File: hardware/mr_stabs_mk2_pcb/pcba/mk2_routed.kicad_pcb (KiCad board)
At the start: 4 copper layers, 93.2 x 35 mm, 73 parts, among them U1 INA228, U2 TPS54202DDC, U3 AP2112K-3.3, U4 BNO055, U5 USBLC6-2SC6, Y1 32.768kHz

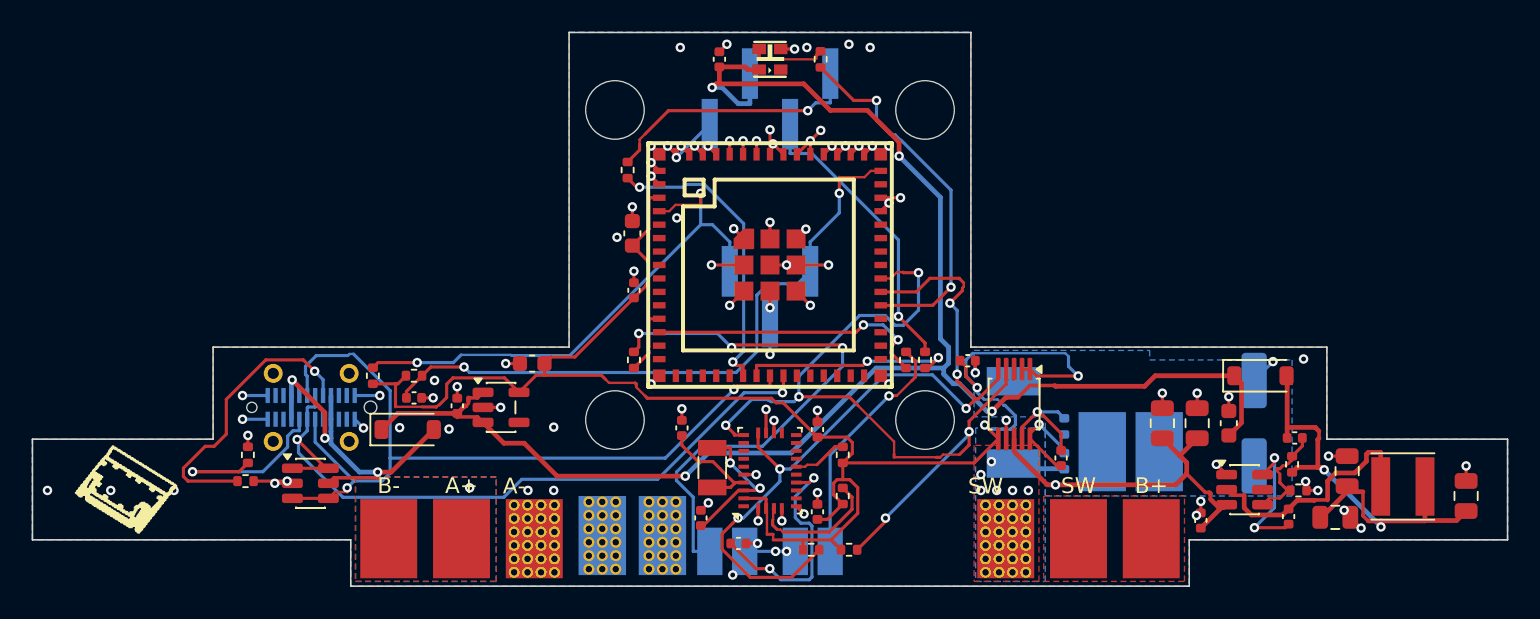
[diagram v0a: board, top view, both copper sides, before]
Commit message: Stand the Nano RX on a right-angle header and align the STEP models
- H2 is now an HX PZ2.54-1x4P WT right-angle SMD header (C46061677) at the stem's rear, pins
  pointing forward; the RX slides on and stands 18 mm toward the wedge. A vertical header would
  have laid it flat. Rotated 180 deg because KiCad mirrors bottom-side footprints and
  legalize.py does not; at 0 deg its pins pointed out past the rear edge.
- EasyEDA's footprints now use their STEP models, offset to match the VRML the renders use
  (align_models.py): the USB-C's STEP sat 2.55 mm low and the headers' 2.5 to 3.8 mm along the
  row, so the exported STEP disagreed with the render.
- New build123d model of the right-angle header; datasheet review for H2.
- Re-routed: 0 errors, 0 unconnected. Order files, STEP and simulations regenerated.

Co-Authored-By: Claude Opus 5.5 <noreply@anthropic.com>
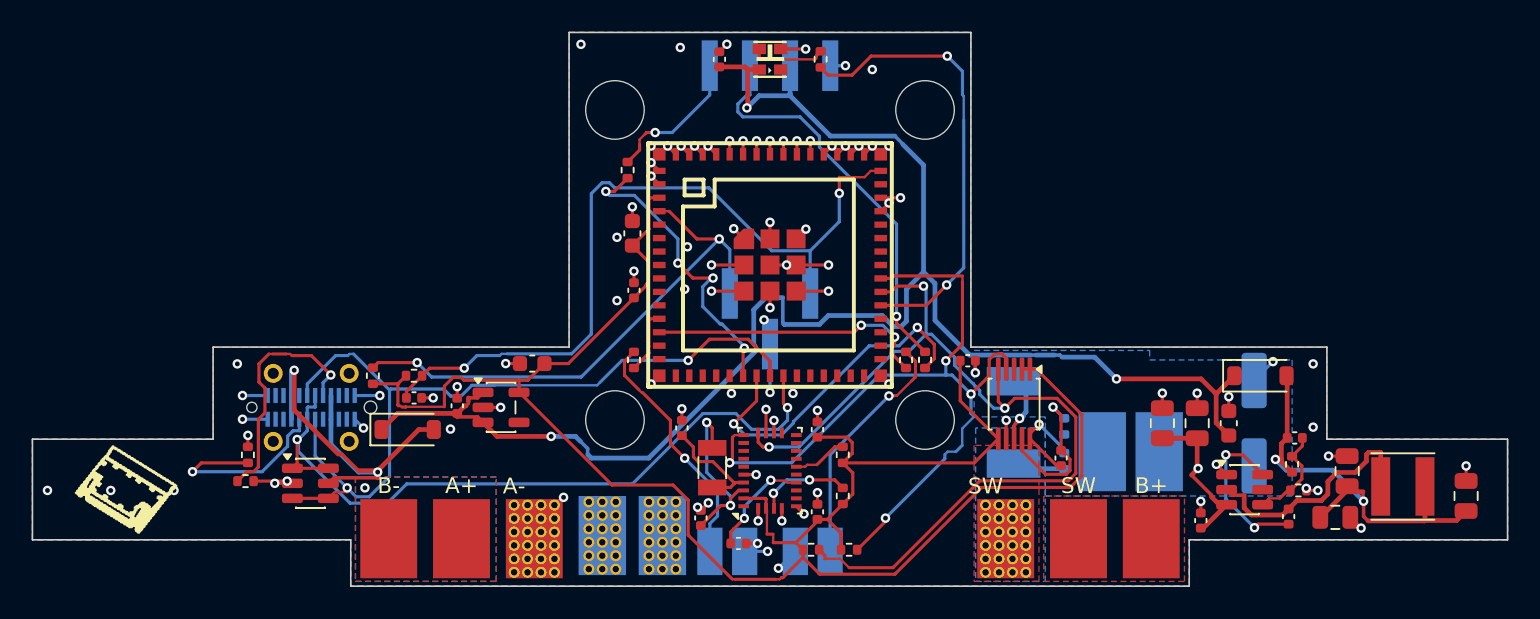
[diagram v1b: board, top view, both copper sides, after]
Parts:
- H2: footprint mk2:CONN-SMD_HX-PZ2.54-1X4P-TP-YQ -> mk2:CONN-SMD_HX-PZ2.54-1X4P-WT
- moved H2 2.10 mm to (100.0, 87.4), turned to 180 degrees
- moved H1 1.40 mm to (100.0, 103.4)
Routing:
- net DSHOT_L: track 35.6 -> 15.5 mm, vias 3 -> 1
- net +3V3: track 108.4 -> 122.4 mm, vias 3 -> 0
- net VBATT: track 22.8 -> 13.3 mm, vias 1 -> 2
- net SCL1: track 49.9 -> 58.3 mm, vias 5 -> 3
- net EN: track 41.0 -> 49.3 mm
- net IO18: track 13.5 -> 21.7 mm
- net IMU_CAP: track 14.9 -> 6.73 mm
- net CRSF_RX_RX: track 16.6 -> 9.19 mm
- net CRSF_RX_TX: track 18.7 -> 25.5 mm
- net IO39: track 23.2 -> 28.8 mm
- net VBUS_USB: track 22.5 -> 27.7 mm, vias 3 -> 2
- net USB_CC2: track 18.5 -> 15.4 mm
- net SENSE_N: track 7.16 -> 9.96 mm
- net IMU_BOOTLOAD: track 8.50 -> 5.92 mm, vias 0 -> 2
- net V5_BUCK: track 30.4 -> 28.0 mm
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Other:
- board text added: "C1"
- board text added: "C2"
- board text added: "NANO RX"
- board text removed: "1"
- board text removed: "2"
- board text removed: "NANO RX: 1=RX TX, 2=RX RX"

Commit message: Move the Mk2 USB-C and bulk cap into the stem; swap to INA238 and TYPE-C-31-D-06
- USB-C and the 100 uF bulk cap sit in the stem between the bosses, away from the motors under
  the ears. BOOT/RST moved to the left ear, the BNO055 block front-right of the USB-C's shell
  legs; two caps went to the wedge face under the parts they serve (no GND via room on top);
  two fixed GND stitching vias keep the stem's bottom pour joined.
- JLCPCB assembly had no INA228 and flagged the 24-pin USB-C as hard to source: INA238
  (C2868250, same pinout, 16-bit) and HRO TYPE-C-31-D-06 (C2689964, 16-pin USB 2.0), both
  reviewed against their datasheets. Paste in the USB-C's shell slots so reflow solders them.
- Re-routed: 0 errors, 0 unconnected. Order files (ORDER.md: PCBA Qty 2), STEP, schematic and
  simulations regenerated.

Firmware: the INA238 needs device ID 0x238, 16-bit reads, ADCRANGE 1 and SHUNT_OHMS 0.0005.

Co-Authored-By: Claude Opus 5.5 <noreply@anthropic.com>
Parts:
- added TP15: GND_STITCH, mk2:StitchVia_0.6mm, F.Cu at (111.6, 102.6)
- added TP16: GND_STITCH, mk2:StitchVia_0.6mm, F.Cu at (88.4, 102.6)
- C19, C22: moved to B.Cu
- U1: value INA228 -> INA238
- USB1: value TYPE-C-31-M-06 -> TYPE-C-31-D-06; footprint mk2:TYPE-C-USB-SMD_TYPE-C-31-M-06 -> mk2:USB-C-SMD_TYPE-C-31-D-06
- moved R16 33.2 mm to (100.0, 112.0)
- moved R15 33.0 mm to (100.0, 110.6), turned to 0 degrees
- moved C3 31.2 mm to (100.0, 104.0), turned to 180 degrees
- moved USB1 29.1 mm to (100.0, 111.1)
- moved U5 26.4 mm to (97.2, 116.1), turned to 180 degrees
- moved H1 21.7 mm to (79.0, 109.0)
- moved C23 11.7 mm to (105.5, 114.0), turned to 0 degrees
- moved C20 10.2 mm to (111.7, 115.9), turned to 180 degrees
- moved C19 9.61 mm to (107.6, 117.2)
- moved U4 8.77 mm to (107.5, 117.6), turned to 180 degrees
- moved Y1 7.62 mm to (103.1, 116.3)
- moved R12 7.60 mm to (111.4, 118.0)
- moved C22 7.51 mm to (103.1, 115.2), turned to 0 degrees
- moved D2 7.11 mm to (84.0, 112.2)
- moved R8 6.22 mm to (98.8, 118.5), turned to 180 degrees
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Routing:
- net USB_DM: track 52.9 -> 16.9 mm
- net SDA1: track 50.4 -> 73.5 mm
- net VBATT: track 13.3 -> 34.5 mm, vias 2 -> 4
- net SCL1: track 58.3 -> 39.0 mm, vias 3 -> 2
- net DSHOT_L: track 15.5 -> 34.1 mm
- net USB_DP: track 46.7 -> 29.3 mm
- net XOUT32: track 7.06 -> 20.4 mm, vias 0 -> 2
- net +3V3: track 122.4 -> 109.5 mm, vias 0 -> 8
- net IO18: track 21.7 -> 13.3 mm
- net +5V: track 103.9 -> 111.8 mm, vias 3 -> 4
- net XIN32: track 11.5 -> 19.2 mm
- net USB_CC2: track 15.4 -> 7.99 mm, vias 1 -> 3
- net GND: track 75.9 -> 69.3 mm, vias 94 -> 99
- net EN: track 49.3 -> 43.1 mm, vias 2 -> 6
- net IMU_BOOTLOAD: track 5.92 -> 1.60 mm, vias 2 -> 0
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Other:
- board text removed: "USB"

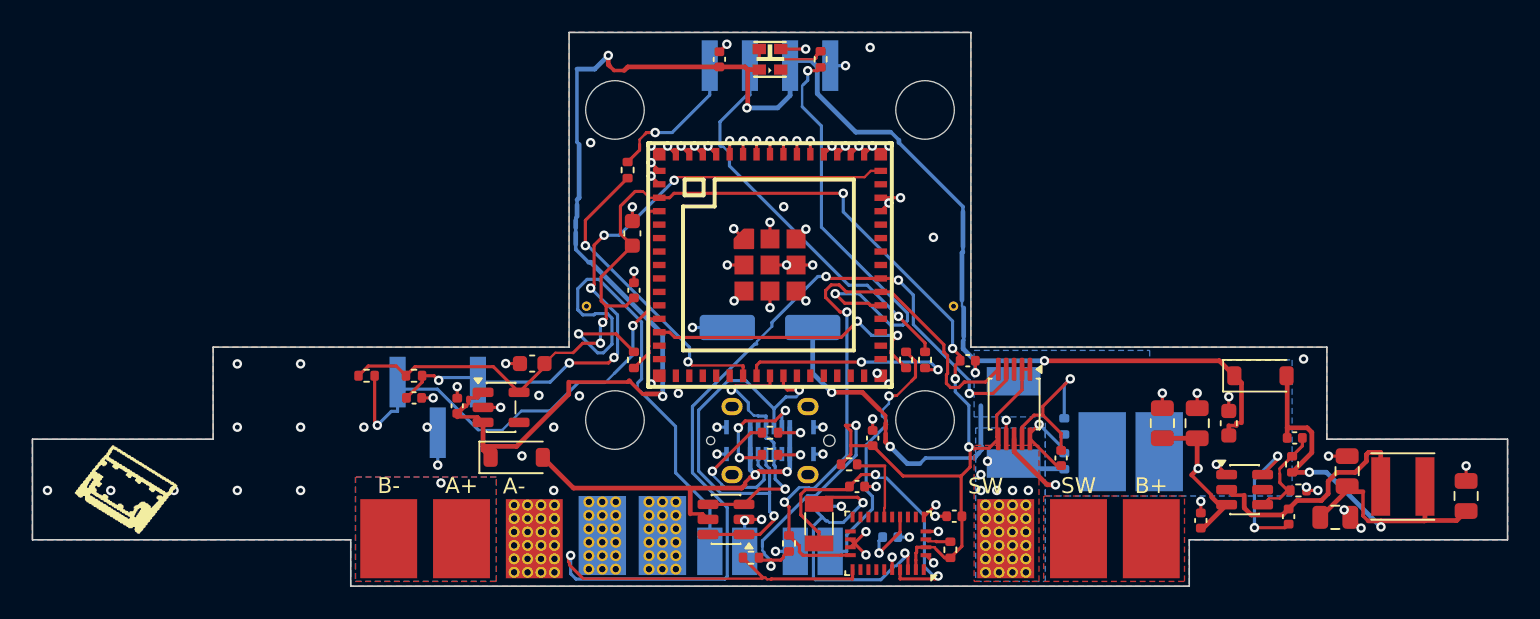
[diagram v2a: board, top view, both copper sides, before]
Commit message: Mk2 board v1.0: inner planes in the gerbers, signature, rounded corners, wired schematic
- gerbers.zip now has In1 and In2. fab.sh exported only F.Cu and B.Cu, so every earlier zip
  for this 4-layer board was missing both GND planes. ORDER.md says to check for 4 copper
  files.
- Silkscreen: "MR STABS MK2" and "v1.0 BEN W 2026" replace the XT60 pad legend on the bottom
  left ear (the roof-face pads keep their own labels), with the BWBots logo above them.
  VERSION in silk.py sets the revision.
- Convex outline corners filleted to 1 mm (corner_radius in gen_placement.py). Placement and
  routing unchanged; zones refilled. DRC 0 errors, 0 unconnected.
- Schematic redrawn as three hierarchical sheets (power, MCU and USB, IMU and radio) with
  nets as wires; connectivity matches mk2.net on all 37 nets.
- STEP, BOM, CPL and renders regenerated from the same board.

Co-Authored-By: Claude Opus 5.5 <noreply@anthropic.com>
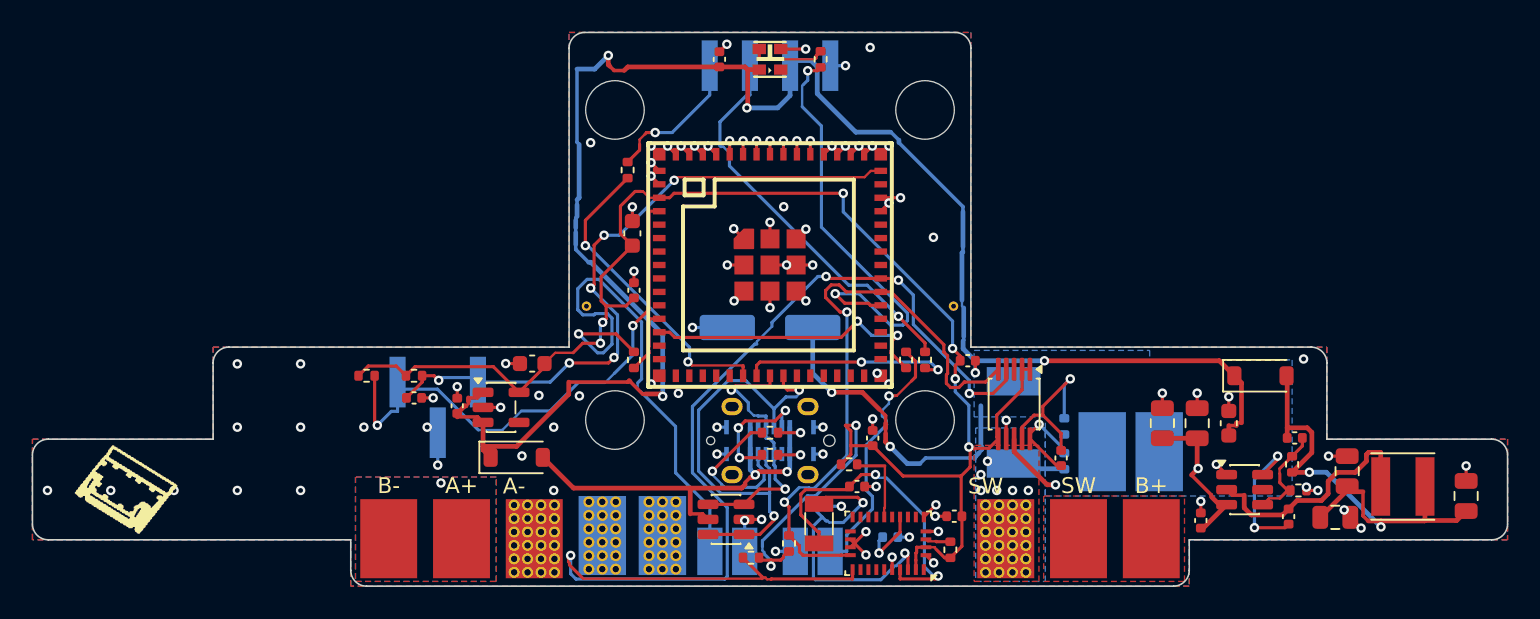
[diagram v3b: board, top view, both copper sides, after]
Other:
- outline, holes or cut-outs redrawn
- board text added: "v1.0 BEN W 2026"
- board text removed: "A-/A+ PACK A"
- board text removed: "B-/B+ PACK B"
- board text removed: "SW/SW SWITCH"
- board text removed: "XT60 PADS, TOP:"

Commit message: Re-route the Mk2 board at JLCPCB's 2 oz rules and fit the CPL rotations
The board orders with 2 oz outer copper, but it was routed at 0.15 mm clearance, a 1 oz
number. Against JLCPCB's 2 oz minimums (0.16 mm track, 0.20 mm space) it had 292 violations
behind a clean DRC. Re-routed at 0.20 mm: 0 errors, 0 unconnected, with mk2_routed.kicad_dru
holding the 2 oz rules so the KiCad GUI checks the same thing.

Getting the stem to route at 0.20 mm took these changes:
- Signal vias 0.5 / 0.25 mm; GND, battery and 5 V vias stay 0.6 / 0.3. Min hole 0.25 mm.
- C3 (100 uF bulk) back on the right ear beside the shunt. Its feed across the stem never
  routed at 2 oz spacing, and a prewired track there walled off the signals. It gives up the
  stem's protection from a dislodged motor.
- INA238 VBUS on BAT_IN, the F pour under the pin. Reads the shunt drop high, at most 35 mV at
  a 70 A stall; current sensing is unchanged.
- B keepouts hold the VBATT pour's neck (shunt to ESC_L+) and R3's Kelvin tap open: signal
  tracks had split the pour and left the ESC current on a track.
- F VBATT patch over the buck input, with the B VBATT pour extended under it so every piece
  stitches down. C6 turned to face it; INA238 moved 0.3 mm off the rear edge.

The copper IR solve now gives a 23.8 mV VBATT drop at 70 A, down from 42.4 mV.

cpl.csv angles and centres are fitted to JLCPCB's own footprint for each LCSC number
(cpl_check.csv). KiCad's angles would have placed C3 reversed and five ICs 90 degrees out.
R5 and U5 no longer have vias in their pads; C14 and C10 still do (open question 8).

Co-Authored-By: Claude Opus 5.5 <noreply@anthropic.com>
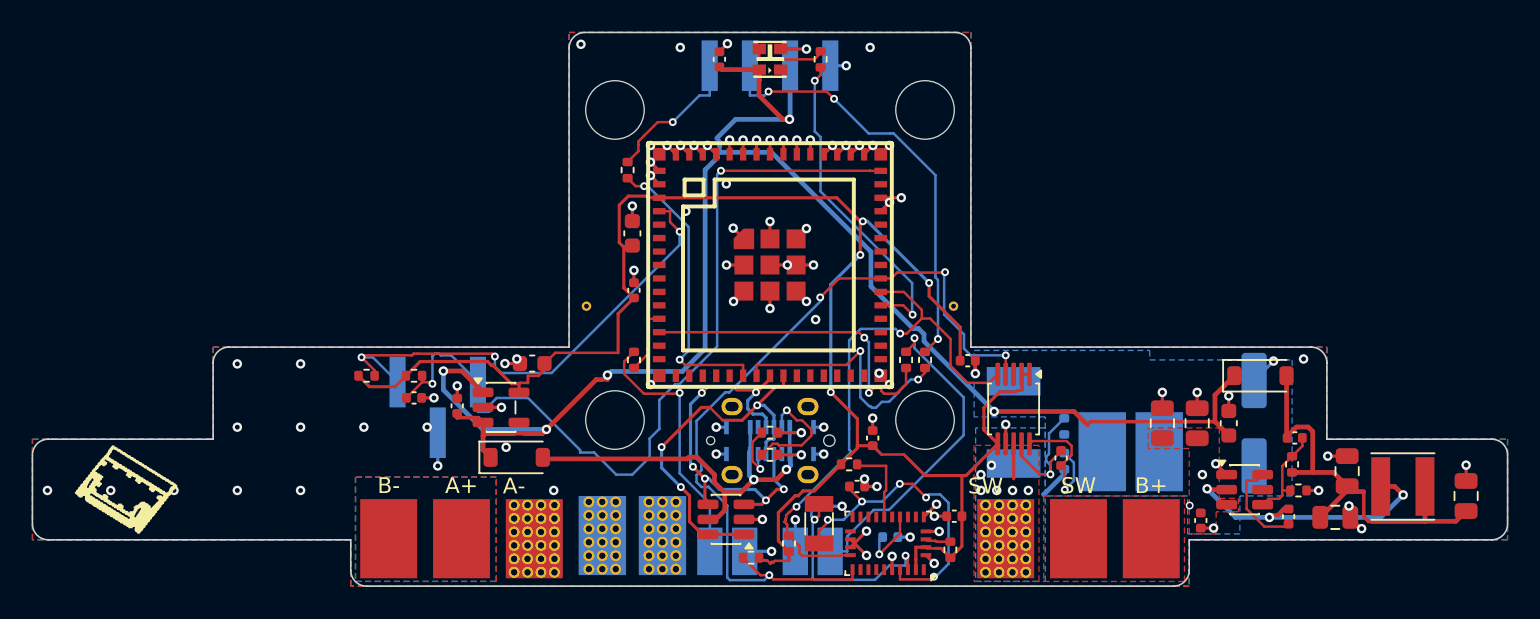
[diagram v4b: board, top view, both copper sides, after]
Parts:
- moved C3 31.2 mm to (130.6, 110.0), turned to 90 degrees
- moved U1 0.31 mm to (115.4, 109.1)
- turned C6 to -90 degrees
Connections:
- U1 pad 8: VBATT -> BAT_IN
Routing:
- net VBATT: track 34.5 -> 0.00 mm, vias 4 -> 2
- net SDA1: track 73.5 -> 51.3 mm
- net DSHOT_L: track 34.1 -> 16.5 mm
- net EN: track 43.1 -> 54.0 mm, vias 6 -> 2
- net USB_DM: track 16.9 -> 26.1 mm, vias 2 -> 6
- net IO39: track 28.3 -> 20.6 mm
- net USB_CC1: track 10.1 -> 3.75 mm
- net XIN32: track 19.2 -> 13.7 mm
- net USB_DP: track 29.3 -> 24.0 mm, vias 2 -> 3
- net +5V: track 111.8 -> 106.6 mm, vias 4 -> 5
- net DSHOT_R: track 16.5 -> 20.6 mm
- net GND: track 69.3 -> 72.9 mm, vias 99 -> 98
- net +3V3: track 109.5 -> 113.1 mm, vias 8 -> 4
- net V5_BUCK: track 30.4 -> 26.9 mm, vias 2 -> 0
- net SCL1: track 39.0 -> 35.8 mm
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- added copper zone on F.Cu, net VBATT
